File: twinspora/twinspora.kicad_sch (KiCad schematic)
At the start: 90 parts, among them J1 TYPE-C-31-M-12, J10 XY-SH1_0-4A61, J12 XY-XH2_54-5A21, J13 Conn_01x02, J2 XT30U-M, J3 XT60PW-M, J4 Conn_01x02, J5 XY-XH2_54-2A21, J6 XY-XH2_54-2A21, J7 Conn_01x02, J8 XY-SH1_0-6A51, J9 XY-SH1_0-6A51, Q1 AO3401A, SW2 TS1187A26020, SW3 TS1187A26020, U1 STM32G473RBTx, U4 XC6206P332MR, U5 CA-IF1044VD-Q1, U8 MT6701QT, U9 MT6701QT, X1 X322512MSB4SI

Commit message: initial completion
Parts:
- removed C33, C34: CL05B104KB54PNC, Basic_Capacitors_Resistors:C0402, symbol Basic_Capacitors_Resistors:CL05B104KB54PNC
- removed J12: XY-XH2_54-5A21, Connector_XH2.54:HDR-TH_5P-P2.50-H-F-W7.0-N, symbol Connector_XH2.54:XY-XH2_54-5A21
- removed J5, J6: XY-XH2_54-2A21, Connector_XH2.54:HDR-TH_2P-P2.50_XY-XH2.54-2A21, symbol Connector_XH2.54:XY-XH2_54-2A21
- removed J8, J9: XY-SH1_0-6A51, Connector_SH1.0:CONN-SMD_6P-P1.00_XY-SH1.0-6A51, symbol Connector_SH1.0:XY-SH1_0-6A51
- removed U8, U9: MT6701QT, Package_DFN_QFN:QFN-16-1EP_3x3mm_P0.5mm_EP1.7x1.7mm, symbol Sensor_Magnetic:MT6701QT
- added C49, C50: 0402CG470J500NT, Basic_Capacitors_Resistors:C0402, symbol Basic_Capacitors_Resistors:0402CG470J500NT
- added J12: XY-SH1_0-5A61, Connector_SH1.0:CONN-SMD_5P-P1.00_XYECONN_XY-SH1.0-5A61, symbol Connector_SH1.0:XY-SH1_0-5A61
- added J5, J6: XY-SH1_0-3A61, Connector_SH1.0:CONN-SMD_3P-P1.00_XYECONN_XY-SH1.0-3A61, symbol Connector_SH1.0:XY-SH1_0-3A61
- added R24, R25: 0402WGF1200TCE, Basic_Capacitors_Resistors:R0402, symbol Basic_Capacitors_Resistors:0402WGF1200TCE
- added TP1, TP10, TP11, TP12, TP13, TP14, TP15, TP16, TP17, TP18, TP19, TP2, TP20, TP21, TP22, TP23, TP24, TP25, TP26, TP27, TP28, TP29, TP3, TP30, TP31, TP32, TP33, TP34, TP35, TP36, TP37, TP38, TP39, TP4, TP40, TP41, TP42, TP43, TP5, TP6, TP7, TP8, TP9: (no value), TestPoint:TestPoint_Pad_D1.0mm, symbol Mechanical:Test_Point
- added U12, U2, U3: SRV05-4A, Package_TO_SOT_SMD:SOT-23-6, symbol Diode:SRV05-4
- H13, H14, H15, H16: footprint footprints/Mechanical:SMD_BD5.6-D3.6 -> Mechanical:SMD_BD5.6-D3.6
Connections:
- net +3.3V: now also TP25.1
- net +5V: now also TP26.1, U3.5 (VP)
- net 5V_BKOUT: now also J12.4, U12.5 (VP)
- net CAN_H: now also J5.3, J6.3
- net CAN_L: now also J5.2, J6.2
- net CAN_VIO: now also TP43.1
- net D+: now also C49.2, U2.1 (IO1), U2.6 (IO4)
- net D-: now also C50.2, U2.3 (IO2), U2.4 (IO3)
- net FDCAN_RX: now also TP18.1
- net FDCAN_TX: now also TP17.1
- net GND: now also C49.1, C50.1, J12.5, J12.6, J12.7, J5.1, J5.4, J5.5, J6.1, J6.4, J6.5, TP27.1, U12.2 (VN), U2.2 (VN), U3.2 (VN)
- net GPIO1: now also J12.3, U12.4 (IO3)
- net GPIO2: now also J12.2, U12.3 (IO2)
- net GPIO3: now also J12.1, U12.1 (IO1)
- net I2C_SCL: now also R25.2, TP30.1, U3.1 (IO1), U3.6 (IO4); no longer J10.4
- net I2C_SDA: now also R24.1, TP29.1, U3.3 (IO2), U3.4 (IO3); no longer J10.3
- net SOA1: now also TP19.1
- net SOA2: now also TP20.1
- net SOB1: now also TP21.1
- net SOB2: now also TP22.1
- net SOC1: now also TP23.1
- net SOC2: now also TP24.1
- net SPI1_MISO: now also TP4.1
- net SPI1_MOSI: now also TP3.1
- net SPI1_NSS: now also TP1.1
- net SPI1_SCK: now also TP2.1
- net SPI2_MISO: now also TP8.1
- net SPI2_MOSI: now also TP7.1
- net SPI2_NSS: now also TP5.1
- net SPI2_SCK: now also TP6.1
- net SPI3_MISO: now also TP12.1
- net SPI3_MOSI: now also TP11.1
- net SPI3_NSS: now also TP9.1
- net SPI3_SCK: now also TP10.1
- net SPI4_MISO: now also TP16.1
- net SPI4_MOSI: now also TP15.1
- net SPI4_NSS: now also TP13.1
- net SPI4_SCK: now also TP14.1
- net TIM1_CH1: now also TP36.1
- net TIM1_CH1N: now also TP35.1
- net TIM1_CH2: now also TP34.1
- net TIM1_CH2N: now also TP33.1
- net TIM1_CH3: now also TP32.1
- net TIM1_CH3N: now also TP31.1
- net TIM8_CH1: now also TP42.1
- net TIM8_CH1N: now also TP41.1
- net TIM8_CH2: now also TP40.1
- net TIM8_CH2N: now also TP39.1
- net TIM8_CH3: now also TP38.1
- net TIM8_CH3N: now also TP37.1
- net VBUS: now also U2.5 (VP)
- net VSENS: now also TP28.1
- new net: J10.4, R25.1
- new net: J10.3, R24.2
- no-connect marks 15 -> 6
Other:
- added sheet magnetic_encoder (magnetic_encoder.kicad_sch)
- added sheet magnetic_encoder1 (magnetic_encoder.kicad_sch)
- note added: "Jumpers (2.54 mm)"
- note added: "Magnetic Encoder - MT6701Q Motor Driver - DRV8316CR"
- note removed: "Encoder 1"
- note removed: "Encoder 2"
- note removed: "Magnetic Encoder MT6701QT"
- note removed: "Motor Driver - DRV8316CR"
- moved on the sheet: C1, C10, C11, C12, C13, C14, C15, C16, C17, C18, C19, C2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

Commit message: designators
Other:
- moved on the sheet: TP1, TP10, TP11, TP12, TP13, TP14, TP15, TP16, TP17, TP18, TP19, TP2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

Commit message: apr 21 push
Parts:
- J13, J7: now not fitted
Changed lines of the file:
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@@
 (kicad_sch
-	(version 20260101)
+	(version 20260306)
 	(generator "eeschema")
 	(generator_version "10.0")
@@
 		)
 		(instances
-			(project ""
+			(project "twinspora"
 				(path "/64e594d2-0aaa-4fb1-a4b5-254d61e53018"
 					(reference "LED1")
@@
 		)
 		(instances
-			(project ""
+			(project "twinspora"
 				(path "/64e594d2-0aaa-4fb1-a4b5-254d61e53018"
 					(reference "C49")
@@
 		)
 		(instances
-			(project ""
+			(project "twinspora"
 				(path "/64e594d2-0aaa-4fb1-a4b5-254d61e53018"
 					(reference "#PWR18")
@@
 		)
 		(instances
-			(project ""
+			(project "twinspora"
 				(path "/64e594d2-0aaa-4fb1-a4b5-254d61e53018"
 					(reference "R4")
@@
 		)
 		(instances
-			(project ""
+			(project "twinspora"
 				(path "/64e594d2-0aaa-4fb1-a4b5-254d61e53018"
 					(reference "J5")
@@
 		)
 		(instances
-			(project ""
+			(project "twinspora"
 				(path "/64e594d2-0aaa-4fb1-a4b5-254d61e53018"
 					(reference "FID1")
@@
 		)
 		(instances
-			(project ""
+			(project "twinspora"
 				(path "/64e594d2-0aaa-4fb1-a4b5-254d61e53018"
 					(reference "U1")
@@
 		)
 		(instances
-			(project ""
+			(project "twinspora"
 				(path "/64e594d2-0aaa-4fb1-a4b5-254d61e53018"
 					(reference "LED2")
@@
 		)
 		(instances
-			(project ""
+			(project "twinspora"
 				(path "/64e594d2-0aaa-4fb1-a4b5-254d61e53018"
 					(reference "TP1")
@@
 		)
 		(instances
-			(project ""
+			(project "twinspora"
 				(path "/64e594d2-0aaa-4fb1-a4b5-254d61e53018"
 					(reference "J4")
@@
 		)
 		(instances
-			(project ""
+			(project "twinspora"
 				(path "/64e594d2-0aaa-4fb1-a4b5-254d61e53018"
 					(reference "J3")
@@
 		)
 		(instances
-			(project ""
+			(project "twinspora"
 				(path "/64e594d2-0aaa-4fb1-a4b5-254d61e53018"
 					(reference "H1")
@@
 		)
 		(instances
-			(project ""
+			(project "twinspora"
 				(path "/64e594d2-0aaa-4fb1-a4b5-254d61e53018"
 					(reference "J2")
@@
 		)
 		(instances
-			(project ""
+			(project "twinspora"
 				(path "/64e594d2-0aaa-4fb1-a4b5-254d61e53018"
 					(reference "R5")
@@
 		)
 		(instances
-			(project ""
+			(project "twinspora"
 				(path "/64e594d2-0aaa-4fb1-a4b5-254d61e53018"
 					(reference "C10")
@@
 		)
 		(instances
-			(project ""
+			(project "twinspora"
 				(path "/64e594d2-0aaa-4fb1-a4b5-254d61e53018"
 					(reference "J6")
@@
 		)
 		(instances
-			(project ""
+			(project "twinspora"
 				(path "/64e594d2-0aaa-4fb1-a4b5-254d61e53018"
 					(reference "R1")
@@
 		)
 		(instances
-			(project ""
+			(project "twinspora"
 				(path "/64e594d2-0aaa-4fb1-a4b5-254d61e53018"
 					(reference "U2")
@@
 		)
 		(instances
-			(project ""
+			(project "twinspora"
 				(path "/64e594d2-0aaa-4fb1-a4b5-254d61e53018"
 					(reference "U5")
@@
 		(on_board yes)
 		(in_pos_files yes)
-		(dnp no)
+		(dnp yes)
 		(property "Reference" "J13"
 			(at 55.88 251.46 0)
@@
 		)
 		(instances
-			(project ""
+			(project "twinspora"
 				(path "/64e594d2-0aaa-4fb1-a4b5-254d61e53018"
 					(reference "X1")
@@
 		)
 		(instances
-			(project ""
+			(project "twinspora"
 				(path "/64e594d2-0aaa-4fb1-a4b5-254d61e53018"
 					(reference "J12")
@@
 		)
 		(instances
-			(project ""
+			(project "twinspora"
 				(path "/64e594d2-0aaa-4fb1-a4b5-254d61e53018"
 					(reference "H13")
@@
 		)
 		(instances
-			(project ""
+			(project "twinspora"
 				(path "/64e594d2-0aaa-4fb1-a4b5-254d61e53018"
 					(reference "J10")
@@
 		(on_board yes)
 		(in_pos_files yes)
-		(dnp no)
+		(dnp yes)
 		(property "Reference" "J7"
 			(at 40.64 224.79 0)
@@
 		)
 		(instances
-			(project ""
+			(project "twinspora"
 				(path "/64e594d2-0aaa-4fb1-a4b5-254d61e53018"
 					(reference "J1")
@@
 		)
 		(instances
-			(project ""
+			(project "twinspora"
 				(path "/64e594d2-0aaa-4fb1-a4b5-254d61e53018"
 					(reference "J11")
@@
 		)
 		(instances
-			(project ""
+			(project "twinspora"
 				(path "/64e594d2-0aaa-4fb1-a4b5-254d61e53018"
 					(page "4")
@@
 		)
 		(instances
-			(project ""
+			(project "twinspora"
 				(path "/64e594d2-0aaa-4fb1-a4b5-254d61e53018"
 					(page "2")

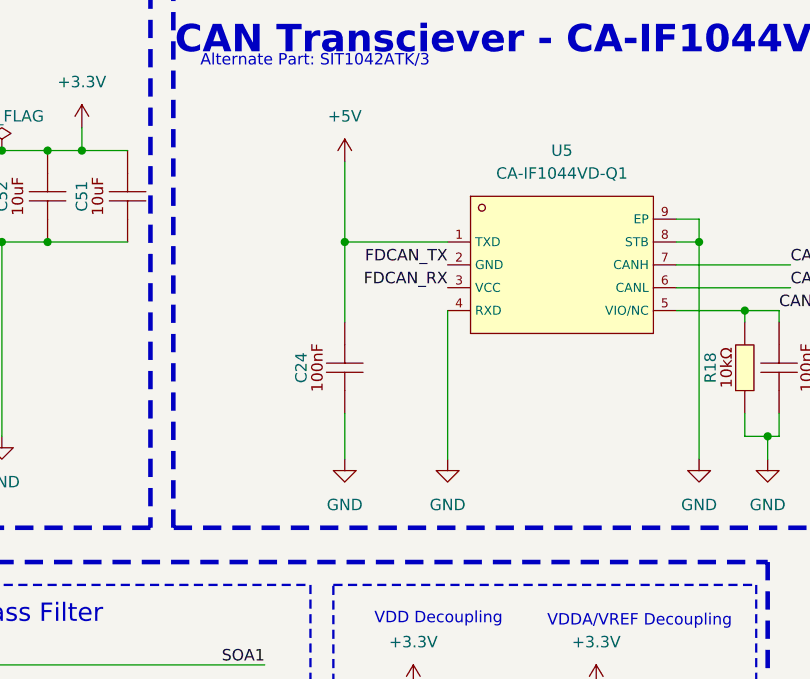
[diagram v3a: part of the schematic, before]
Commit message: CAN wrong pinout
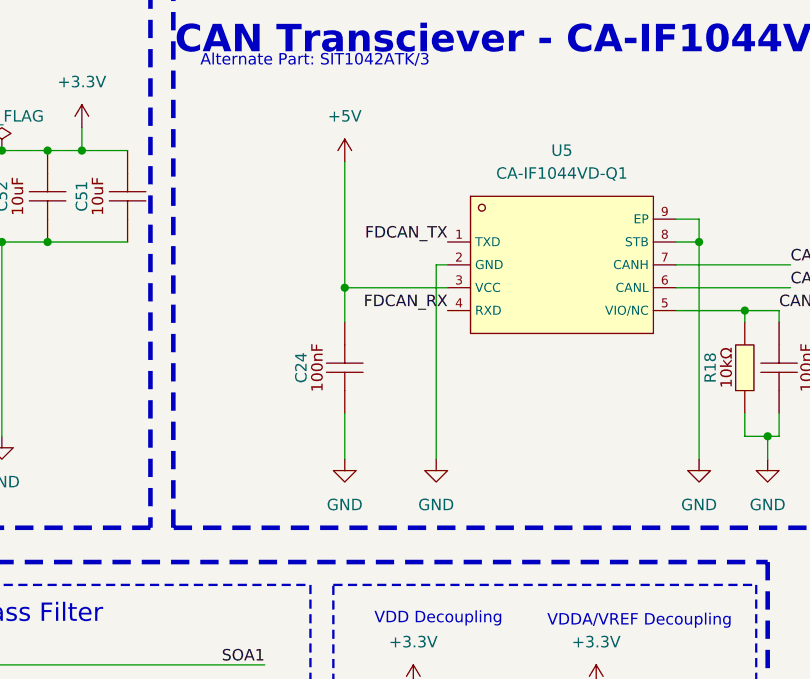
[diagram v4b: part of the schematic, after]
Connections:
- net +5V: now also U5.3 (VCC); no longer U5.1 (TXD)
- net FDCAN_RX: now also U5.4 (RXD); no longer U5.3 (VCC)
- net FDCAN_TX: now also U5.1 (TXD); no longer U5.2 (GND)
- net GND: now also U5.2 (GND); no longer U5.4 (RXD)
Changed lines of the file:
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@@
 	)
 	(junction
-		(at 322.58 41.91)
-		(diameter 0)
-		(color 0 0 0 0)
-	)
-	(junction
 		(at 340.36 139.7)
 		(diameter 0)
@@
 	)
 	(junction
+		(at 322.58 46.99)
+		(diameter 0)
+		(color 0 0 0 0)
+	)
+	(junction
 		(at 119.38 36.83)
 		(diameter 0)
@@
 	(wire
 		(pts
+			(xy 332.74 44.45) (xy 332.74 66.04)
+		)
+		(stroke
+			(width 0)
+			(type default)
+		)
+	)
+	(wire
+		(pts
 			(xy 144.78 59.69) (xy 144.78 66.04)
 		)
@@
 	(wire
 		(pts
-			(xy 322.58 41.91) (xy 334.01 41.91)
+			(xy 334.01 44.45) (xy 332.74 44.45)
 		)
 		(stroke
@@
 	(wire
 		(pts
-			(xy 322.58 41.91) (xy 322.58 50.8)
+			(xy 322.58 33.02) (xy 322.58 46.99)
 		)
 		(stroke
@@
 	(wire
 		(pts
+			(xy 322.58 46.99) (xy 322.58 50.8)
+		)
+		(stroke
+			(width 0)
+			(type default)
+		)
+	)
+	(wire
+		(pts
 			(xy 361.95 41.91) (xy 361.95 66.04)
 		)
@@
 	(wire
 		(pts
-			(xy 369.57 63.5) (xy 369.57 66.04)
+			(xy 322.58 46.99) (xy 334.01 46.99)
 		)
 		(stroke
@@
 	(wire
 		(pts
-			(xy 322.58 33.02) (xy 322.58 41.91)
+			(xy 369.57 63.5) (xy 369.57 66.04)
 		)
 		(stroke
@@
 	(wire
 		(pts
-			(xy 334.01 49.53) (xy 334.01 66.04)
-		)
-		(stroke
-			(width 0)
-			(type default)
-		)
-	)
-	(wire
-		(pts
 			(xy 147.32 97.79) (xy 147.32 101.6)
 		)
@@
 		)
 	)
-	(label "FDCAN_TX"
-		(at 334.01 44.45 180)
-		(effects
-			(font
-				(size 1.27 1.27)
-			)
-			(justify right bottom)
-		)
-	)
 	(label "TIM8_CH2N"
 		(at 77.47 172.72 180)
@@
 		)
 	)
-	(label "FDCAN_RX"
-		(at 334.01 46.99 180)
-		(effects
-			(font
-				(size 1.27 1.27)
-			)
-			(justify right bottom)
-		)
-	)
 	(label "SPI3_NSS"
 		(at 31.75 129.54 180)
@@
 		)
 	)
+	(label "FDCAN_TX"
+		(at 334.01 41.91 180)
+		(effects
+			(font
+				(size 1.27 1.27)
+			)
+			(justify right bottom)
+		)
+	)
 	(label "TIM8_CH1N"
 		(at 77.47 177.8 180)
@@
 		)
 	)
+	(label "FDCAN_RX"
+		(at 334.01 49.53 180)
+		(effects
+			(font
+				(size 1.27 1.27)
+			)
+			(justify right bottom)
+		)
+	)
 	(label "SPI3_MISO"
 		(at 31.75 124.46 180)
@@
 	(symbol
 		(lib_id "power:GND")
-		(at 334.01 66.04 0)
+		(at 332.74 66.04 0)
+		(mirror y)
 		(unit 1)
 		(body_style 1)
@@
 		(in_pos_files yes)
 		(dnp no)
-		(fields_autoplaced yes)
 		(property "Reference" "#PWR30"
-			(at 334.01 72.39 0)
+			(at 332.74 72.39 0)
 			(hide yes)
 			(show_name no)
@@
 		)
 		(property "Value" "GND"
-			(at 334.01 71.12 0)
+			(at 332.74 71.12 0)
 			(show_name no)
 			(do_not_autoplace no)
@@
 		)
 		(property "Footprint" ""
-			(at 334.01 66.04 0)
+			(at 332.74 66.04 0)
 			(hide yes)
 			(show_name no)
@@
 		)
 		(property "Datasheet" ""
-			(at 334.01 66.04 0)
+			(at 332.74 66.04 0)
 			(hide yes)
 			(show_name no)
@@
 		)
 		(property "Description" "Power symbol creates a global label with name \"GND\" , ground"
-			(at 334.01 66.04 0)
+			(at 332.74 66.04 0)
 			(hide yes)
 			(show_name no)

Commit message: NEW
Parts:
- removed H10, H11, H12, H9: MountingHole_Pad, symbol Mechanical:MountingHole_Pad
- removed J12: XY-SH1_0-5A61, Connector_SH1.0:CONN-SMD_5P-P1.00_XYECONN_XY-SH1.0-5A61, symbol Connector_SH1.0:XY-SH1_0-5A61
- removed J2: XT30U-M, Connector_AMASS:AMASS_XT30PW-M_1x02_P2.50mm_Horizontal, symbol Connector_Amass:XT30U-M
- removed J3: XT60PW-M, Connector_AMASS:AMASS_XT60PW-M_1x02_P7.20mm_Horizontal, symbol Connector_Amass:XT60PW-M
- removed J4: Conn_01x02, Connector_Phoenix_MSTB:PhoenixContact_MSTBA_2,5_2-G_1x02_P5.00mm_Horizontal, symbol Connector_Generic:Conn_01x02
- removed R1: 0402WGF5101TCE, Basic_Capacitors_Resistors:R0402, symbol Basic_Capacitors_Resistors:0402WGF5101TCE
- removed SW2, SW3: TS1187A26020, Switch:SW-SMD_4P-L5.2-W5.2-1, symbol Switch:TS1187A26020
- removed U12: SRV05-4A, Package_TO_SOT_SMD:SOT-23-6, symbol Diode:SRV05-4
- added D4: 1N4148WS, Diode_SMD:D_SOD-323, symbol Diode:1N4148WS
- added J12: XY-SH1_0-3A61, Connector_SH1.0:CONN-SMD_3P-P1.00_XYECONN_XY-SH1.0-3A61, symbol Connector_SH1.0:XY-SH1_0-3A61
- added LED3: KT-0603W, LED:LED0603-R-RD_WHITE, symbol LED:KT-0603W
- added R1: 0402WGF3300TCE, Resistor_SMD:R_0402_1005Metric, symbol Basic_Capacitors_Resistors:0402WGF3300TCE
- added R32, R33: 0402WGF1002TCE, Resistor_SMD:R_0402_1005Metric, symbol Basic_Capacitors_Resistors:0402WGF1002TCE
- added R34: 0402WGF5101TCE, Resistor_SMD:R_0402_1005Metric, symbol Basic_Capacitors_Resistors:0402WGF5101TCE
- added SW1, SW2: SKSGPAE010, Switch_UWRL:SW-SMD_SKSGAAE010, symbol Switch_UWRL:SKSGPAE010
- added U13: WSD4066DN, Transistor_FET_UWRL:DFN-8_L3.2-W3.1-P0.65-LS3.4-BL-EP, symbol Transistor_FET_UWRL:WSD4066DN
- added U14: FMMT620TA, Transistor_BJT_UWRL:SOT-23-3_L2.9-W1.6-P1.90-LS2.8-BR, symbol Transistor_BJT_UWRL:FMMT620TA
- added U15, U16: BK22C07-4DP/2-0_4V(800), Connector_HRS_BK22:CONN-SMD_4P-P0.40_BAM04-08073-0414, symbol Connector_HRS_BK22:BK22C07-4DP/2-0_4V(800)
- C1, C10, C11, C12, C13, C14, C15, C16, C17, C18, C19, C2, C22, C23, C24, C3, C4, C53, C6, C7, C8, C9: footprint Basic_Capacitors_Resistors:C0402 -> Capacitor_SMD:C_0402_1005Metric
- C49, C50: footprint Basic_Capacitors_Resistors:C0402 -> Capacitor_SMD:C_0402_1005Metric; now not fitted
- C5: footprint Basic_Capacitors_Resistors:C0603 -> Capacitor_SMD:C_0603_1608Metric
- C51, C52: footprint Basic_Capacitors_Resistors:C0805 -> Capacitor_SMD:C_0805_2012Metric
- H5: footprint (none) -> MountingHole:MountingHole_2.2mm_M2
- J13, J7: footprint Connector_PinSocket_2.54mm:PinSocket_1x02_P2.54mm_Vertical -> (none)
- R10, R11, R12, R13, R14, R15, R16, R17, R18, R2, R23, R24, R25, R3, R4, R5, R6, R7, R8, R9: footprint Basic_Capacitors_Resistors:R0402 -> Resistor_SMD:R_0402_1005Metric
- U2, U3: footprint Package_TO_SOT_SMD:SOT-23-6 -> lemon-pepper-footprints:SOT-23-6
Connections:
- net +3.3V: now also LED1.1 (A), SW2.1, SW2.3
- net 5V_BKOUT: now also J12.2
- net BOOT: now also SW2.2, SW2.4
- net CAN_H: now also R17.2, U15.1, U15.4, U16.1, U16.4; no longer R17.1
- net CAN_L: now also U15.2, U15.3, U16.2, U16.3
- net GND: now also R2.2, J12.1, J12.4, J12.5, R1.2, R32.1, R34.2, SW1.2, SW1.4, SW1.5, SW1.6, SW2.5, SW2.6, U15.11, U15.12, U15.7, U15.8, U16.11, U16.12, U16.7, U16.8; no longer LED1.2 (K), LED2.1 (K)
- net GPIO3: now also J12.3
- net RESET: now also SW1.1, SW1.3
- net USER_LED: now also LED2.2 (A); no longer R2.1
- net VCC: now also LED3.1 (A), U13.10 (D2), U13.5 (D2), U13.6 (D2), U13.7 (D1), U13.8 (D1), U13.9 (D1)
- net at J7.2 (Pin_2): now also R17.1; no longer R17.2
- new net: LED2.1 (K), R2.1
- new net: R32.2, U14.1 (B)
- new net: R33.1, U13.2 (G1), U13.4 (G2), U14.3 (C)
- new net: LED3.2 (K), R34.1
- new net: LED1.2 (K), R1.1
- new net: D4.2 (A), U14.2 (E)
- new net +BATT: D4.1 (K), U13.1 (S1), U13.3 (S2), U15.10, U15.5, U15.6, U15.9, U16.10, U16.5, U16.6, U16.9
- new net VCP: R33.2
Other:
- sheet motor_driver ports: added VCP, nFAULT; removed none
- sheet motor_driver1 ports: added VCP, nFAULT; removed none
- note added: "*See TI DRV 8316 EVM for inspiration/source"
- note added: "POWER IN"
- note added: "Reverse Polarity Protection"
- note removed: "Alternative Power Connector (pick one)"
- note removed: "P=5.00mm Screw Terminal"
- note removed: "PWR IN"
- moved on the sheet: H13, H14, H15, H16, J11, J13, J7, R17, R23
